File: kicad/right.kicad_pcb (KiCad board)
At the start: 4 copper layers, 137.5 x 109.3 mm, 114 parts, among them Q1 PMF170XP,115, Q2 FS8205A_C2830320, SW1 TS-1088-AR02016, U1 SN74LVC1G17DBVR, U10 SN74LVC1G74DQER, U2 E73-2G4M08S1C, U4 S2B-PH-K-S(LF)(SN), U5 BL8573CS8TR, U6 DW01A_C42380662, U7 LP5024RSMR, U8 MAX17048, U9 USBLC6-2SC6, X1 FC-13532.768KHZ9PF20PPM

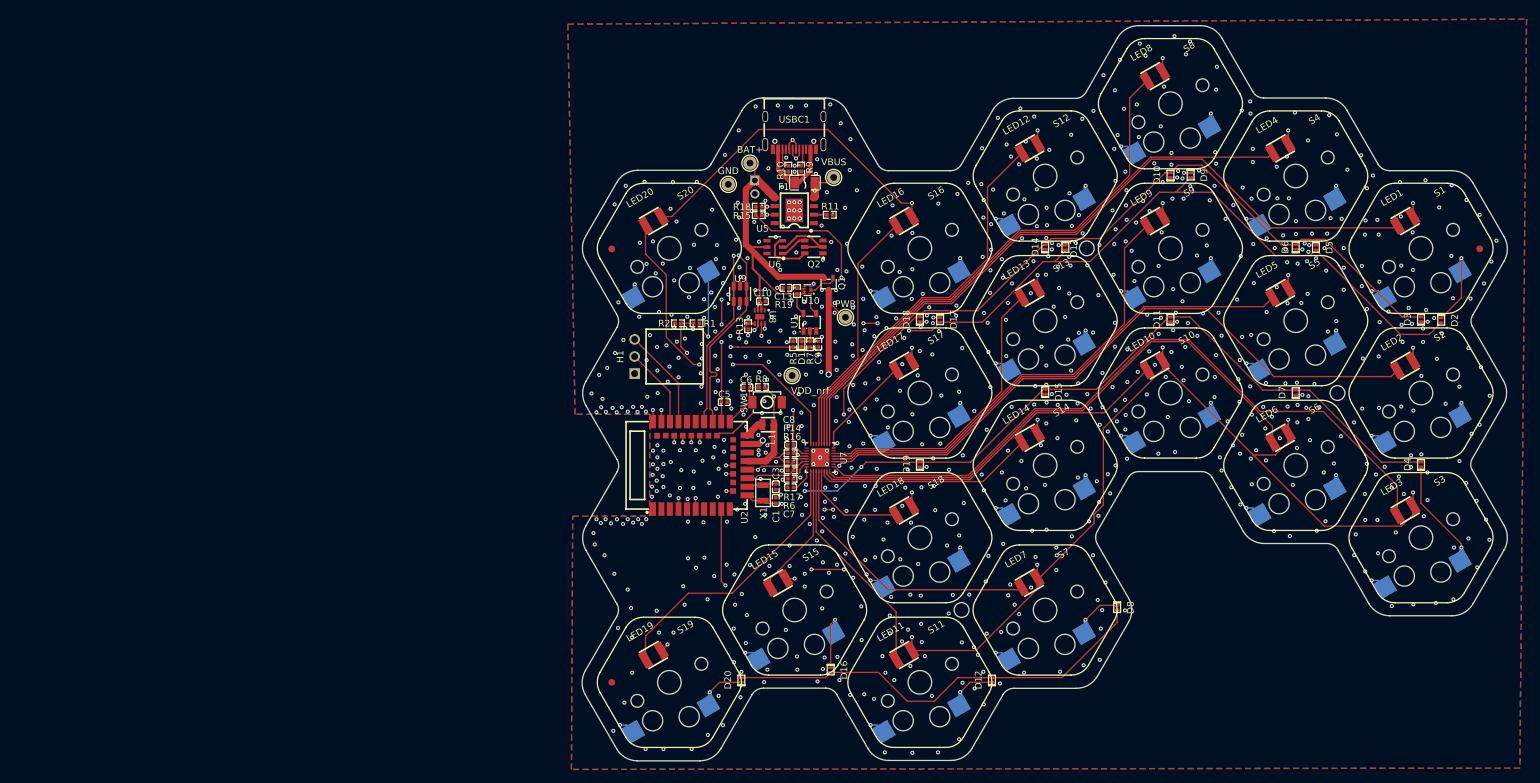
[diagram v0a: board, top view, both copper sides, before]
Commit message: docs: update charger protection and bring-up checklist
- document selectable 96.5 kΩ and 102 kΩ charge-current settings
- add USB-C TVS and 1.5 A polyfuse protection details
- update IP2312U charger and DW01A protection wiring
- mark completed schematic and ERC checklist items
- revise PCB placement, routing, BOM, and bring-up procedures
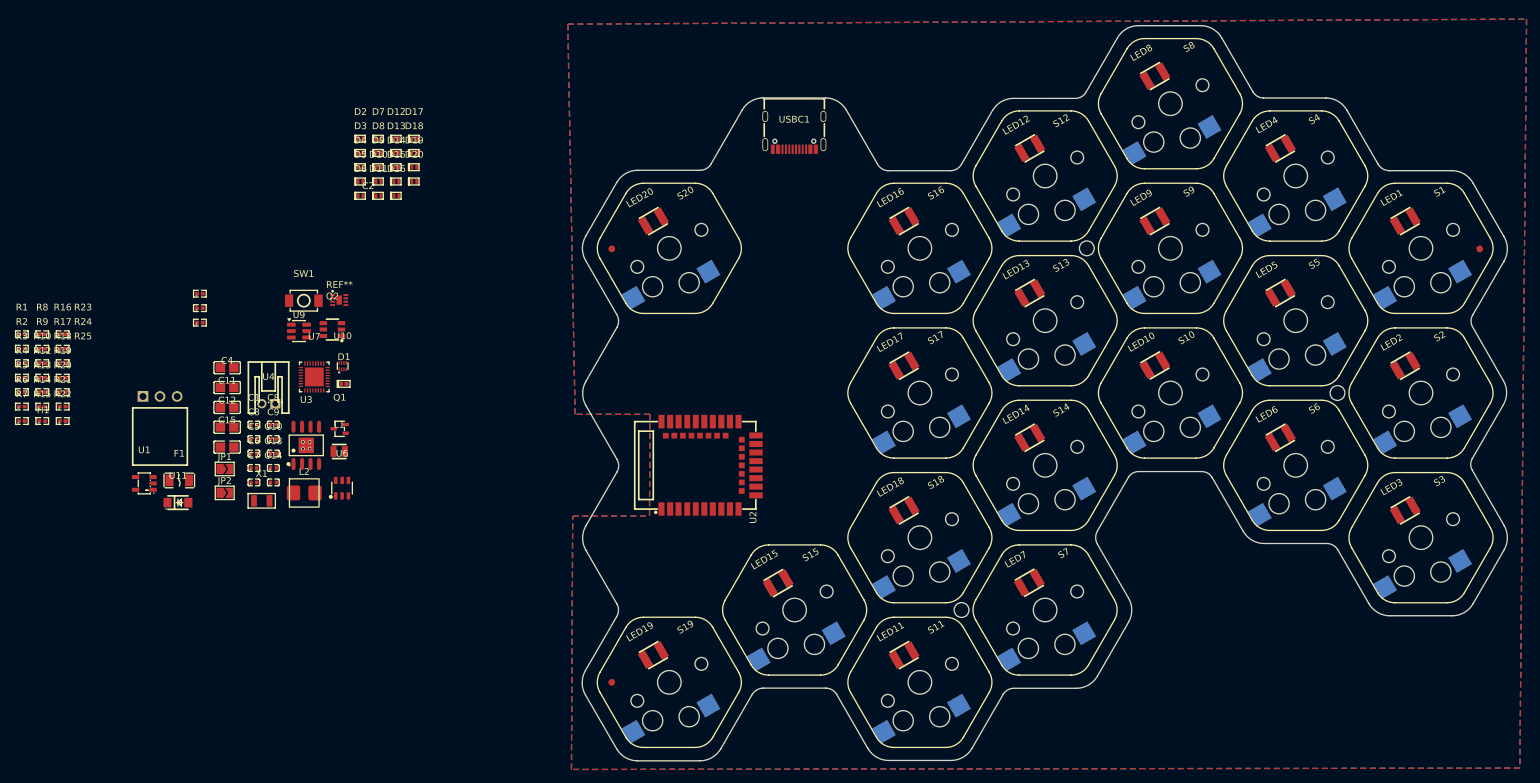
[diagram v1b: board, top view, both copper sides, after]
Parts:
- removed BAT+, GND, PWR, VBUS, VDD_nrf: TestPoint_THTPad_D2.0mm_Drill1.0mm, TestPoint:TestPoint_THTPad_D2.0mm_Drill1.0mm
- removed R11: RC0402FR-07680RL, easyeda2kicad:R0402
- removed U5: BL8573CS8TR, easyeda2kicad:ESOP-8_L4.9-W3.9-P1.27-LS6.0-BL-EP
- added C11: 22uF, easyeda2kicad:C0805, F.Cu at (-16.8, 75.8)
- added C12: 22uF, easyeda2kicad:C0805, F.Cu at (-16.8, 78.7)
- added C14: CL05B104KB54PNC, easyeda2kicad:C0402, F.Cu at (-9.93, 86.9)
- added C15: 22uF, easyeda2kicad:C0805, F.Cu at (-16.8, 81.7)
- added C2: 22uF, easyeda2kicad:C0805, F.Cu at (-16.8, 69.9)
- added C4: 22uF, easyeda2kicad:C0805, F.Cu at (-16.8, 72.8)
- added JP1: 96.5k, Jumper:SolderJumper-2_P1.3mm_Open_TrianglePad1.0x1.5mm, F.Cu at (-17.2, 84.9)
- added JP2: 102k, Jumper:SolderJumper-2_P1.3mm_Open_TrianglePad1.0x1.5mm, F.Cu at (-17.2, 88.5)
- added L2: ~, Library:BCIHP0420SC-1R0M, F.Cu at (-5.33, 88.5)
- added R12: 0.5Ω, easyeda2kicad:R0402, F.Cu at (-44.3, 71.3)
- added R20: 1k, easyeda2kicad:R0402, F.Cu at (-41.2, 73.5)
- added R21: 1k, easyeda2kicad:R0402, F.Cu at (-41.2, 75.7)
- added R22: 102k, easyeda2kicad:R0402, F.Cu at (-41.2, 77.8)
- added R23: 102k, easyeda2kicad:R0402, F.Cu at (-20.8, 58.9)
- added R24: 1k, easyeda2kicad:R0402, F.Cu at (-20.8, 61.0)
- added R25: 1k, easyeda2kicad:R0402, F.Cu at (-20.8, 63.2)
- added R3: 102k, easyeda2kicad:R0402, F.Cu at (-47.3, 69.2)
- added R4: 96.5k, easyeda2kicad:R0402, F.Cu at (-47.3, 71.3)
- added U11: SMF5.0A, easyeda2kicad:SOD-123FL_L2.8-W1.8-LS3.6-RD, F.Cu at (-24.1, 89.9)
- added U3: IP2312, easyeda2kicad:SOP-8_L4.9-W3.9-P1.27-LS6.0-BL-EP, F.Cu at (-5.03, 81.4)
- R15, R18: value 0402WGF1002TCE -> 0.5Ω
- U4: moved to F.Cu
- moved D4 163.7 mm to (3.03, 40.1), turned to 0 degrees
- moved D2 162.9 mm to (3.03, 35.8), turned to 0 degrees
- moved D3 159.5 mm to (3.03, 38.0), turned to 0 degrees
- moved D5 142.3 mm to (3.03, 42.2), turned to 0 degrees
- moved D7 141.5 mm to (5.69, 35.8), turned to 0 degrees
- moved D6 139.2 mm to (3.03, 44.3), turned to 0 degrees
- moved D8 128.9 mm to (5.69, 38.0), turned to 0 degrees
- moved D9 120.7 mm to (5.69, 40.1), turned to 0 degrees
- moved D12 119.6 mm to (8.35, 35.8), turned to 0 degrees
- moved D11 119.1 mm to (5.69, 44.3), turned to 0 degrees
- moved D10 117.7 mm to (5.69, 42.2), turned to 0 degrees
- moved R7 117.7 mm to (-47.3, 77.8), turned to 0 degrees
- moved R9 115.9 mm to (-44.3, 67.0), turned to 0 degrees
- moved R5 114.8 mm to (-47.3, 73.5), turned to 0 degrees
- moved R6 114.8 mm to (-47.3, 75.7), turned to 0 degrees
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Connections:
- net Net-(U2-DCH) renamed /DCCH
- Q2 pad 2: Net-(U6-VM) -> unconnected-(Q2-D1/D2-Pad2)
- Q2 pad 3: GND -> /BAT-
- Q2 pad 5: Net-(U6-VM) -> unconnected-(Q2-D1/D2-Pad5)
- R15 pad 1: /CHRG -> Net-(R12-Pad2)
- R15 pad 2: /VDD_nRF -> Net-(C4-Pad2)
- R18 pad 1: /STDBY -> /BAT+
- R18 pad 2: /VDD_nRF -> Net-(U3-BAT)
- U2 pad 41: /CHRG -> unconnected-(U2-NF1-Pad41)
- U2 pad 43: /STDBY -> unconnected-(U2-NF2-Pad43)
- U4 pad 2: GND -> /BAT-
- U6 pad 5: /BAT+ -> Net-(U6-VDD)
- U6 pad 6: GND -> /BAT-
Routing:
- net /PWR: track 596.5 -> 0.00 mm, vias 22 -> 0
- net /COL2: track 255.1 -> 0.00 mm, vias 5 -> 0
- net /COL3: track 211.3 -> 0.00 mm, vias 5 -> 0
- net /COL1: track 211.2 -> 0.00 mm, vias 4 -> 0
- net /COL4: track 176.3 -> 0.00 mm, vias 5 -> 0
- net /ROW2: track 143.5 -> 0.00 mm, vias 4 -> 0
- net /ROW1: track 139.2 -> 0.00 mm, vias 4 -> 0
- net /ROW3: track 123.4 -> 0.00 mm, vias 3 -> 0
- net /COL5: track 122.0 -> 0.00 mm, vias 7 -> 0
- net /LED1: track 109.8 -> 0.00 mm
- net /LED3: track 105.8 -> 0.00 mm
- net /LED2: track 97.8 -> 0.00 mm
- net /ROW4: track 90.9 -> 0.00 mm, vias 2 -> 0
- net /LED4: track 88.1 -> 0.00 mm
- net /BAT+: track 84.1 -> 0.00 mm, vias 1 -> 0
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
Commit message: finished right part. changed inductor for charger, changed resistor for driver, and added some caps.
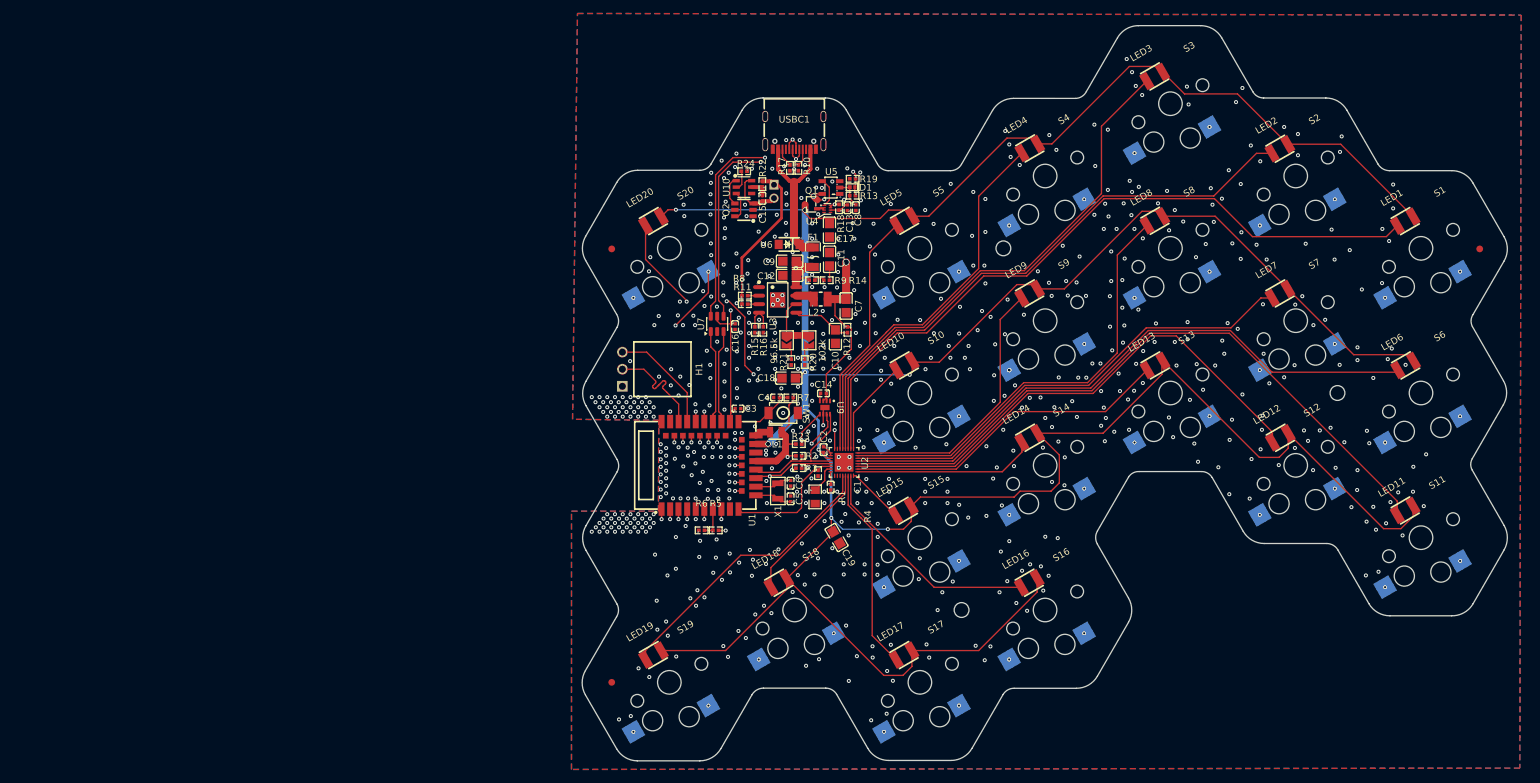
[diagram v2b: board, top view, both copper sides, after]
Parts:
- removed D10, D11, D12, D13, D14, D15, D16, D17, D18, D19, D2, D20, D3, D4, D5, D6, D7, D8, D9: CDSQC4148-HF, easyeda2kicad:X1-DFN1006-2_L1.0-W0.6-RD
- removed R25: 1k, easyeda2kicad:R0402
- removed U11: SMF5.0A, easyeda2kicad:SOD-123FL_L2.8-W1.8-LS3.6-RD
- added C16: CL05B104KB54PNC, easyeda2kicad:C0402, F.Cu at (58.7, 63.8)
- added C17: 22uF, easyeda2kicad:C0805, F.Cu at (72.7, 49.5)
- added C18: 22uF, easyeda2kicad:C0805, F.Cu at (66.7, 71.4)
- added C19: 22uF, easyeda2kicad:C0805, F.Cu at (73.8, 95.1)
- added R11: 1k, easyeda2kicad:R0402, F.Cu at (60.1, 60.4)
- added U5: SN74LVC1G17DBVR, easyeda2kicad:SOT-23-5_L3.0-W1.7-P0.95-LS2.8-BR, F.Cu at (73.0, 43.1)
- C1: value 0402CG120J500NT -> CL05A105KA5NQNC
- C10: value CL05B104KB54PNC -> 22uF; footprint easyeda2kicad:C0402 -> easyeda2kicad:C0805
- C15, C4: value 22uF -> CL05B104KB54PNC; footprint easyeda2kicad:C0805 -> easyeda2kicad:C0402
- C2: value 22uF -> CL05A105KA5NQNC; footprint easyeda2kicad:C0805 -> easyeda2kicad:C0402
- C3: value 0402CG120J500NT -> ZRB15XR61A475KE01D
- C5: value ZRB15XR61A475KE01D -> 0402CG120J500NT
- C6: value CL05B104KB54PNC -> 0402CG120J500NT
- C7, C9: value CL05A105KA5NQNC -> 22uF; footprint easyeda2kicad:C0402 -> easyeda2kicad:C0805
- JP1: value 96.5k -> 102k
- JP2: value 102k -> 96.5k
- L2: value ~ -> 1uH; footprint Library:BCIHP0420SC-1R0M -> easyeda2kicad:IND-SMD_L2.5-W2.0
- R1: value 0402WGF1004TCE -> 14k7 1% 0805; footprint easyeda2kicad:R0402 -> easyeda2kicad:R0805
- R13: value 0402WGF1002TCE -> RTT022614FTH
- R14, R9: value 0402WGF5101TCE -> 0.5Ω
- R15: value 0.5Ω -> 102k
- R16: value 0402WGF5101TCE -> 102k
- R17: value 0402WGF1004TCE -> 0402WGF5101TCE
- R18: value 0.5Ω -> 0402WGF1002TCE
- R2: value WR04W2494FTL -> 0402WGF5101TCE
- R20: value 1k -> 102k
- R21: value 1k -> 96.5k
- R22: value 102k -> 1k
- R23: value 102k -> 0402WGF1002TCE
- R3: value 102k -> 0402WGF5101TCE
- R4: value 96.5k -> 0402WGF1004TCE
- R5: value 0402WGF1002TCE -> 0402WGF1004TCE
- R6: value ERA2AED753X -> WR04W2494FTL
- R7: value RTT022614FTH -> 0402WGF1002TCE
- R8: value 0402WGF1002TCE -> 1k
- S1, S10, S11, S12, S13, S14, S15, S16, S17, S18, S19, S2, S20, S3, S4, S5, S6, S7, S8, S9: footprint hexcaps:PG1350_hotswap -> hexcaps:PG1350_hotswap_reversed
- U1: value SN74LVC1G17DBVR -> E73-2G4M08S1C; footprint easyeda2kicad:SOT-23-5_L3.0-W1.7-P0.95-LS2.8-BR -> easyeda2kicad:WIRELM-SMD_E73-2G4M08S1C
- U10: value SN74LVC1G74DQER -> DW01A_C42380662; footprint easyeda2kicad:X2SON-8_L1.4-W1.0-P0.35-BL -> easyeda2kicad:SOT-23-6_L2.9-W1.6-P0.95-LS2.9-BL
- U2: value E73-2G4M08S1C -> LP5024RSMR; footprint easyeda2kicad:WIRELM-SMD_E73-2G4M08S1C -> easyeda2kicad:VQFN-32_L4.0-W4.0-P0.40-TL-EP
- U4: value S2B-PH-K-S(LF)(SN) -> SN74LVC1G74DQER; footprint easyeda2kicad:CONN-TH_S2B-PH-K-S-LF-SN -> easyeda2kicad:X2SON-8_L1.4-W1.0-P0.35-BL
- U6: value DW01A_C42380662 -> SMF5.0A; footprint easyeda2kicad:SOT-23-6_L2.9-W1.6-P0.95-LS2.9-BL -> easyeda2kicad:SOD-123FL_L2.8-W1.8-LS3.6-RD
- U7: value LP5024RSMR -> USBLC6-2SC6; footprint easyeda2kicad:VQFN-32_L4.0-W4.0-P0.40-TL-EP -> Package_TO_SOT_SMD:SOT-23-6
- U8: value MAX17048 -> S2B-PH-K-S(LF)(SN); footprint PCM_SparkFun-Semiconductor-Standard:DFN-8_2x2mm_P0.5mm_EP1.2x0.8mm -> easyeda2kicad:CONN-TH_S2B-PH-K-S-LF-SN; moved to B.Cu
- U9: value USBLC6-2SC6 -> MAX17048; footprint Package_TO_SOT_SMD:SOT-23-6 -> PCM_SparkFun-Semiconductor-Standard:DFN-8_2x2mm_P0.5mm_EP1.2x0.8mm
- moved R13 123.9 mm to (76.2, 44.3), turned to 180 degrees
- moved R19 121.1 mm to (76.2, 41.8), turned to 180 degrees
- moved R1 120.4 mm to (70.6, 89.1), turned to -90 degrees
- moved R12 119.9 mm to (75.4, 64.2), turned to -90 degrees
- moved R4 119.2 mm to (71.0, 85.5), turned to -90 degrees
- moved R14 118.1 mm to (72.3, 56.9)
- moved R18 117.7 mm to (74.2, 46.0), turned to 90 degrees
- moved R2 116.6 mm to (68.2, 83.0), turned to 180 degrees
- moved R3 116.5 mm to (68.2, 84.8), turned to 180 degrees
- moved R10 116.1 mm to (68.1, 40.2), turned to -90 degrees
- moved R9 114.9 mm to (70.1, 56.9)
- moved R7 114.3 mm to (66.9, 74.3), turned to 180 degrees
- moved R17 111.4 mm to (66.8, 40.2), turned to -90 degrees
- moved R20 110.4 mm to (69.0, 69.0), turned to -90 degrees
- moved R22 109.8 mm to (62.8, 42.6), turned to 90 degrees
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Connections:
- C1 pad 1: Net-(U2-XL1) -> Net-(U2-VCAP)
- C10 pad 1: /BAT+ -> GND
- C10 pad 2: GND -> Net-(U3-BAT)
- C11 pad 2: Net-(U3-BAT) -> Net-(C11-Pad2)
- C12 pad 2: /BAT+ -> /VBUS
- C13 pad 2: Net-(U10-~{CLR}) -> Net-(U4-~{CLR})
- C14 pad 1: Net-(U6-VDD) -> /BAT+
- C14 pad 2: /BAT- -> GND
- C15 pad 1: GND -> Net-(U10-VDD)
- C15 pad 2: /VBUS -> /BAT-
- C2 pad 1: GND -> /PWR
- C2 pad 2: /VBUS -> GND
- C3 pad 1: Net-(U2-XL2) -> /VBUS
- C4 pad 1: GND -> /RESET
- C4 pad 2: Net-(C4-Pad2) -> GND
- C5 pad 1: /VBUS -> Net-(U1-XL1)
- C6 pad 1: /RESET -> Net-(U1-XL2)
- C7 pad 1: Net-(U7-VCAP) -> GND
- C7 pad 2: GND -> /BAT+
- C8 pad 1: /PWR -> Net-(U5-A)
- C9 pad 1: Net-(U1-A) -> GND
- C9 pad 2: GND -> /VBUS
- D1 pad 2: Net-(U1-A) -> Net-(U5-A)
- L2 pad 1: Net-(U3-SW) -> /BAT+
- L2 pad 2: /BAT+ -> Net-(U3-SW)
- R1 pad 1: /PWR_BTN_PRESS -> Net-(U2-IREF)
- R1 pad 2: /PWR_BTN -> GND
- R10 pad 1: Net-(USBC1-CC2) -> Net-(USBC1-CC1)
- R12 pad 1: /VBUS -> /BAT+
- R12 pad 2: Net-(R12-Pad2) -> Net-(U3-BAT)
- R13 pad 1: /BAT_ALTR -> /PWR_BTN
- R13 pad 2: /VDD_nRF -> Net-(U5-A)
- R14 pad 1: /SDA -> Net-(R14-Pad1)
- R14 pad 2: /VDD_nRF -> Net-(C11-Pad2)
- R15 pad 1: Net-(R12-Pad2) -> GND
- R15 pad 2: Net-(C4-Pad2) -> Net-(U3-NTC)
- R16 pad 1: /SCL -> GND
- R16 pad 2: /VDD_nRF -> Net-(U3-NTC)
- R17 pad 1: /LED_EN -> Net-(USBC1-CC2)
- R18 pad 1: /BAT+ -> Net-(U4-~{CLR})
- R18 pad 2: Net-(U3-BAT) -> /BAT+
- R19 pad 1: Net-(U10-~{CLR}) -> /PWR_BTN
- R19 pad 2: /BAT+ -> GND
- R2 pad 1: GND -> /SDA
- R2 pad 2: /PWR_BTN_PRESS -> /VDD_nRF
- R20 pad 1: /BAT+ -> Net-(JP1-B)
- R20 pad 2: Net-(U3-TEST) -> GND
- R21 pad 1: Net-(U6-VDD) -> Net-(JP2-B)
- R21 pad 2: /BAT+ -> GND
- R22 pad 1: GND -> Net-(U10-VDD)
- R22 pad 2: Net-(U3-NTC) -> /BAT+
- R23 pad 1: GND -> /BAT_ALTR
- R23 pad 2: Net-(U3-NTC) -> /VDD_nRF
- R24 pad 2: Net-(U6-VM) -> Net-(U10-VM)
- R3 pad 1: Net-(JP2-B) -> /SCL
- R3 pad 2: GND -> /VDD_nRF
- R4 pad 1: Net-(JP1-B) -> /LED_EN
- R5 pad 1: /PWR_BTN -> /PWR_BTN_PRESS
- R5 pad 2: GND -> /PWR_BTN
- R6 pad 1: Net-(U7-IREF) -> GND
- R6 pad 2: GND -> /PWR_BTN_PRESS
- R7 pad 1: /PWR_BTN -> /VDD_nRF
- R7 pad 2: Net-(U1-A) -> /RESET
- R8 pad 1: /VDD_nRF -> /BAT+
- R8 pad 2: /RESET -> Net-(U3-TEST)
- R9 pad 1: Net-(USBC1-CC1) -> /VBUS
- R9 pad 2: GND -> Net-(R14-Pad1)
- S1 pad 1: /COL1 -> /S1
- S1 pad 2: Net-(D2-Pad1) -> GND
- S10 pad 1: /COL3 -> /S10
- S10 pad 2: Net-(D11-Pad1) -> GND
- S11 pad 1: /COL3 -> /S11
- S11 pad 2: Net-(D12-Pad1) -> GND
- S12 pad 1: /COL4 -> /S12
- S12 pad 2: Net-(D13-Pad1) -> GND
- S13 pad 1: /COL4 -> /S13
- S13 pad 2: Net-(D14-Pad1) -> GND
- S14 pad 1: /COL4 -> /S14
- S14 pad 2: Net-(D15-Pad1) -> GND
- S15 pad 1: /COL4 -> /S15
- S15 pad 2: Net-(D16-Pad1) -> GND
- S16 pad 1: /COL5 -> /S16
- S16 pad 2: Net-(D17-Pad1) -> GND
- S17 pad 1: /COL5 -> /S17
- S17 pad 2: Net-(D18-Pad1) -> GND
- S18 pad 1: /COL5 -> /S18
- S18 pad 2: Net-(D19-Pad1) -> GND
- S19 pad 1: /COL5 -> /S19
- S19 pad 2: Net-(D20-Pad1) -> GND
- S2 pad 1: /COL1 -> /S2
- S2 pad 2: Net-(D3-Pad1) -> GND
- S3 pad 1: /COL1 -> /S3
- S3 pad 2: Net-(D4-Pad1) -> GND
- S4 pad 1: /COL2 -> /S4
- S4 pad 2: Net-(D5-Pad1) -> GND
- S5 pad 1: /COL2 -> /S5
- S5 pad 2: Net-(D6-Pad1) -> GND
- S6 pad 1: /COL2 -> /S6
- S6 pad 2: Net-(D7-Pad1) -> GND
- S7 pad 1: /COL2 -> /S7
- S7 pad 2: Net-(D8-Pad1) -> GND
- S8 pad 1: /COL3 -> /S8
- S8 pad 2: Net-(D9-Pad1) -> GND
- S9 pad 1: /COL3 -> /S9
- S9 pad 2: Net-(D10-Pad1) -> GND
- U1 pad 1: unconnected-(U1-N.C-Pad1) -> /S19
- U1 pad 2: Net-(U1-A) -> /S18
- U1 pad 3: GND -> /S17
- U1 pad 4: Net-(U1-Y) -> /S16
- U1 pad 5: /BAT+ -> GND
- U10 pad 1: Net-(U1-Y) -> Net-(Q2-G2)
- U10 pad 2: /PMOS_gate -> Net-(U10-VM)
- U10 pad 3: /PMOS_gate -> Net-(Q2-G1)
- U10 pad 4: GND -> unconnected-(U10-NC-Pad4)
- U10 pad 5: unconnected-(U10-Q-Pad5) -> Net-(U10-VDD)
- U10 pad 6: Net-(U10-~{CLR}) -> /BAT-
- U2 pad 10: /ROW2 -> /LED13
- U2 pad 11: Net-(U2-XL1) -> /LED12
- U2 pad 12: /ROW3 -> /LED11
- U2 pad 13: Net-(U2-XL2) -> /LED6
- U2 pad 14: unconnected-(U2-P0.06-Pad14) -> /LED7
- U2 pad 15: /LED_EN -> /LED8
- U2 pad 16: /SDA -> /LED9
- U2 pad 17: /SCL -> /LED10
- U2 pad 18: /BAT_ALTR -> /LED1
- U2 pad 19: /VDD_nRF -> /LED2
- U2 pad 20: unconnected-(U2-P12-Pad20) -> /LED3
- U2 pad 21: GND -> /LED4
- U2 pad 22: unconnected-(U2-P0.07-Pad22) -> /LED5
- U2 pad 23: /PWR -> unconnected-(U2-OUT22-Pad23)
- U2 pad 24: GND -> /LED20
- U2 pad 25: /DCCH -> GND
- U2 pad 26: /RESET -> GND
- U2 pad 27: /VBUS -> /PWR
- U2 pad 28: /ROW1 -> /SDA
- U2 pad 29: /D- -> /SCL
- U2 pad 30: unconnected-(U2-P17-Pad30) -> /LED_EN
- U2 pad 31: /D+ -> Net-(U2-IREF)
- U2 pad 32: /COL4 -> Net-(U2-VCAP)
- U2 pad 33: unconnected-(U2-P0.13-Pad33) -> GND
- U2 pad 4: /PWR_BTN_PRESS -> /LED19
- U2 pad 5: GND -> /LED18
- U2 pad 6: /COL5 -> /LED17
- U2 pad 7: unconnected-(U2-AI0-Pad7) -> /LED16
- U2 pad 8: unconnected-(U2-AI5-Pad8) -> /LED15
- U2 pad 9: /ROW4 -> /LED14
- U4 pad 1: /BAT+ -> Net-(U4-CLK)
- U4 pad 2: /BAT- -> /PMOS_gate
- U6 pad 1: Net-(Q2-G2) -> /VBUS_RAW
- U6 pad 2: Net-(U6-VM) -> GND
- U7 pad 1: /LED19 -> /D+
- U7 pad 2: /LED15 -> GND
- U7 pad 3: /LED11 -> /D-
- U7 pad 4: /LED7 -> /USB_D-
- U7 pad 5: /LED18 -> /VBUS
- U7 pad 6: /LED14 -> /USB_D+
- U8 pad 1: GND -> /BAT+
- U8 pad 2: /BAT+ -> /BAT-
- U9 pad 1: /D+ -> GND
- U9 pad 2: GND -> /BAT+
- U9 pad 3: /D- -> /BAT+
- U9 pad 4: /D- -> GND
- U9 pad 5: /VBUS -> /BAT_ALTR
- U9 pad 6: /D+ -> GND
- USBC1 pad A6: /D+ -> /USB_D+
- USBC1 pad A7: /D- -> /USB_D-
- USBC1 pad B6: /D+ -> /USB_D+
- USBC1 pad B7: /D- -> /USB_D-
- X1 pad 1: Net-(U2-XL1) -> Net-(U1-XL1)
- X1 pad 2: Net-(U2-XL2) -> Net-(U1-XL2)
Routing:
- net /PWR: track 0.00 -> 520.8 mm, vias 0 -> 8
- net /S11: track 0.00 -> 126.9 mm, vias 0 -> 2
- net /S1: track 0.00 -> 120.2 mm, vias 0 -> 2
- net /S6: track 0.00 -> 112.4 mm, vias 0 -> 2
- net /LED1: track 0.00 -> 105.7 mm
- net /S2: track 0.00 -> 105.1 mm, vias 0 -> 2
- net /LED11: track 0.00 -> 100.6 mm
- net /BAT+: track 0.00 -> 100.3 mm, vias 0 -> 6
- net /S7: track 0.00 -> 99.8 mm, vias 0 -> 2
- net /S12: track 0.00 -> 93.9 mm, vias 0 -> 2
- net /S3: track 0.00 -> 91.7 mm, vias 0 -> 2
- net /LED6: track 0.00 -> 91.0 mm
- net /LED2: track 0.00 -> 87.3 mm
- net /PWR_BTN: track 0.00 -> 82.6 mm, vias 0 -> 4
- net /LED3: track 0.00 -> 79.5 mm
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
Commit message: cleaned right half, added test points, and some datasheets to the project
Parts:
- added TP1: BAT+, TestPoint:TestPoint_Pad_D2.0mm, B.Cu at (60.6, 41.5)
- added TP10: PM_GATE, TestPoint:TestPoint_Pad_D2.0mm, F.Cu at (69.7, 48.5)
- added TP11: DFF_CLK, TestPoint:TestPoint_Pad_D2.0mm, F.Cu at (72.8, 40.0)
- added TP2: BAT-, TestPoint:TestPoint_Pad_D2.0mm, B.Cu at (61.9, 44.5)
- added TP3: GND, TestPoint:TestPoint_Pad_D2.0mm, B.Cu at (61.1, 53.8)
- added TP4: VBUS, TestPoint:TestPoint_Pad_D2.0mm, B.Cu at (63.5, 50.0)
- added TP5: PWR, TestPoint:TestPoint_Pad_D2.0mm, B.Cu at (71.8, 52.2)
- added TP6: 3V3, TestPoint:TestPoint_Pad_D2.0mm, B.Cu at (70.9, 88.2)
- added TP7: PWR_PRESS, TestPoint:TestPoint_Pad_D2.0mm, F.Cu at (54.1, 96.6)
- added TP8: SDA, TestPoint:TestPoint_Pad_D2.0mm, B.Cu at (60.7, 89.9)
- added TP9: SCL, TestPoint:TestPoint_Pad_D2.0mm, B.Cu at (62.0, 94.2)
- moved REF** 48.9 mm to (43.9, 100.0)
- moved REF** 12.5 mm to (111.1, 52.1)
- moved G** 7.93 mm to (60.9, 64.7)
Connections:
- net /SWBCLK renamed /SWDCLK
- net /VDD_nRF renamed /3V3
- net Net-(U4-CLK) renamed /DFF_CLK
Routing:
- net /SCL: track 29.6 -> 37.8 mm
- net /SDA: track 21.0 -> 29.1 mm, vias 0 -> 1
- net /PWR: track 520.8 -> 528.8 mm, vias 8 -> 10
- net /3V3: track 21.5 -> 26.5 mm
- net /BAT+: track 100.3 -> 105.1 mm
- net /VBUS_RAW: track 24.1 -> 28.8 mm, vias 0 -> 1
- net /PWR_BTN_PRESS: track 4.41 -> 7.47 mm
- net /BAT-: track 9.91 -> 12.6 mm
- net /PMOS_gate: track 2.26 -> 4.97 mm
- net /DFF_CLK: track 4.43 -> 7.07 mm
- net /S8: track 77.9 -> 80.3 mm
- net /S7: track 99.8 -> 102.2 mm
- net /S2: track 105.1 -> 106.9 mm
- net /S1: track 120.2 -> 122.0 mm
- net /S13: track 66.2 -> 64.9 mm
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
